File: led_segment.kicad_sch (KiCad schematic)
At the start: 8 parts, among them Q7 BC857

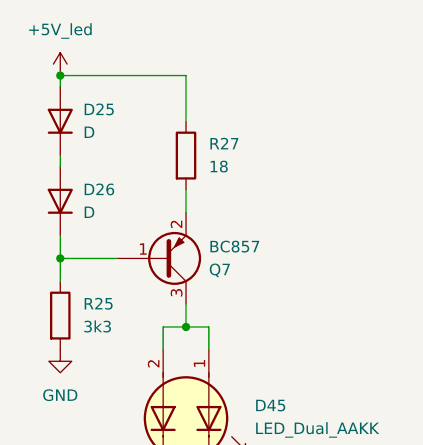
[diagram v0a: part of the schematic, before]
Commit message: current source diodes specified
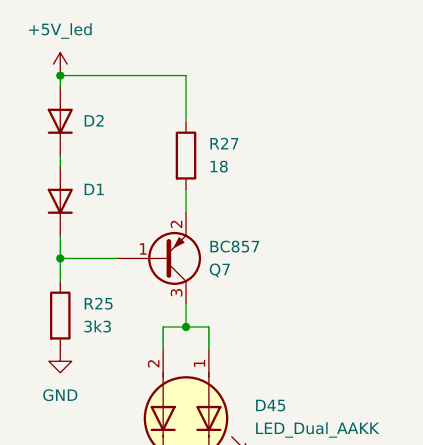
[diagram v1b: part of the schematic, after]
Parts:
- removed D25, D26: D, Diode_SMD:D_0603_1608Metric, symbol Device:D
- added D1, D2: 1N4148, Diode_THT:D_DO-35_SOD27_P7.62mm_Horizontal, symbol Diode:1N4148
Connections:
- net +5V_led: now also D2.2 (A)
- net at Q7.1 (B), R25.1: now also D1.1 (K)
- new net: D1.2 (A), D2.1 (K)

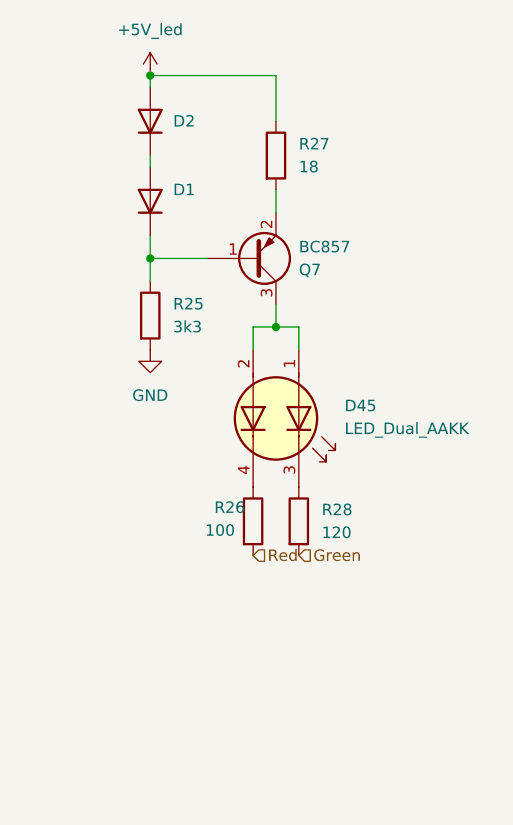
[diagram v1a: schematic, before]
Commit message: Schematic sites change
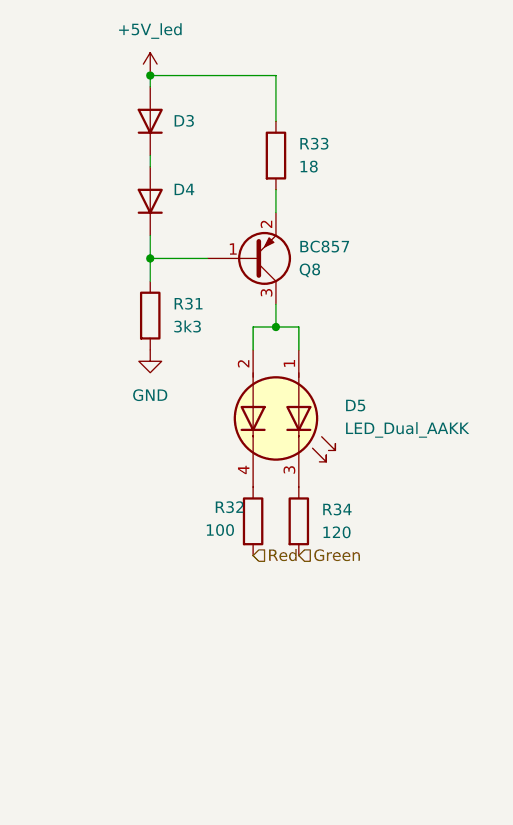
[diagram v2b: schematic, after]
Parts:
- D3: renamed from D2; footprint Diode_THT:D_DO-35_SOD27_P7.62mm_Horizontal -> Diode_SMD:D_SOD-123
- D4: renamed from D1; footprint Diode_THT:D_DO-35_SOD27_P7.62mm_Horizontal -> Diode_SMD:D_SOD-123
- renumbered D45 to D5, Q7 to Q8, R25 to R31, R26 to R32, R27 to R33, R28 to R34

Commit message: mos leds drivers
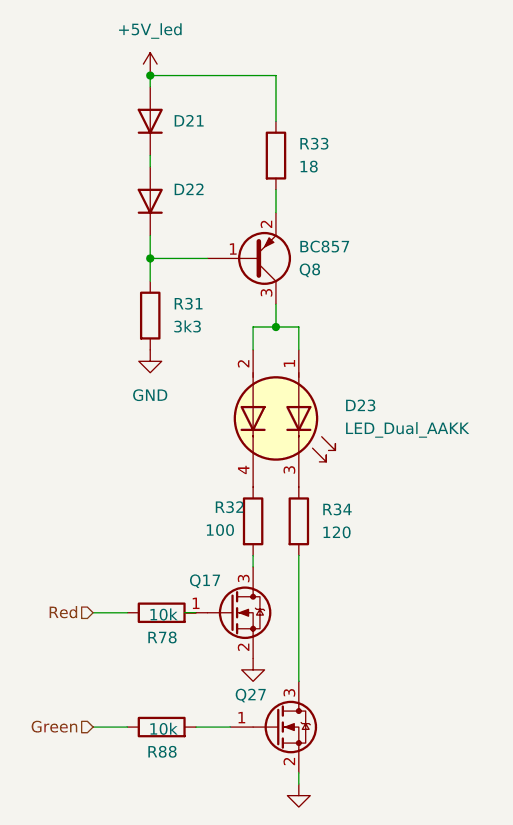
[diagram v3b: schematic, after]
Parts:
- added Q17, Q27: 2N7002H, Package_TO_SOT_SMD:SOT-23, symbol Transistor_FET:2N7002H
- added R78, R88: 10k, Resistor_SMD:R_0603_1608Metric, symbol Device:R
- renumbered D3 to D21, D4 to D22, D5 to D23
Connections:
- net GND: now also Q17.2 (S), Q27.2 (S)
- net Green: now also R88.1; no longer R34.2
- net Red: now also R78.1; no longer R32.2
- new net: Q17.1 (G), R78.2
- new net: Q17.3 (D), R32.2
- new net: Q27.1 (G), R88.2
- new net: Q27.3 (D), R34.2

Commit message: New current source and external mosfet keys for leds
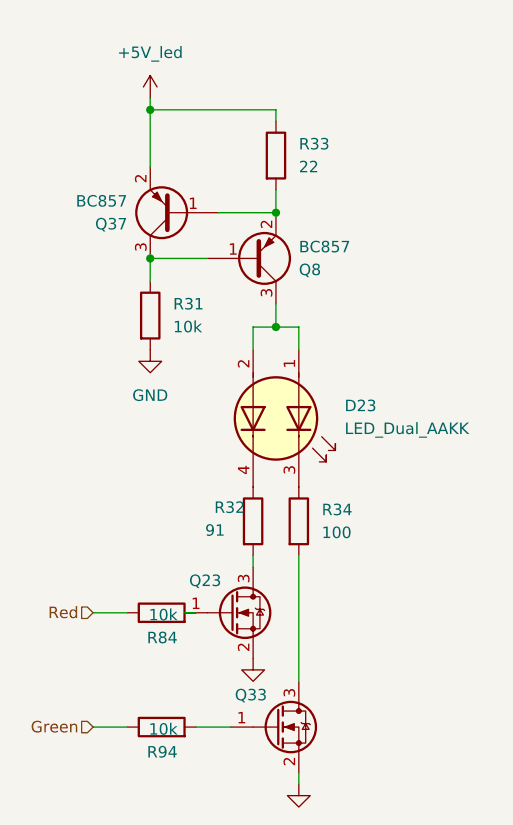
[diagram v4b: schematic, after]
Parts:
- removed D21, D22: 1N4148, Diode_SMD:D_SOD-123, symbol Diode:1N4148
- added Q37: BC857, Package_TO_SOT_SMD:SOT-23, symbol Transistor_BJT:BC857
- R31: value 3k3 -> 10k
- R32: value 100 -> 91
- R33: value 18 -> 22
- R34: value 120 -> 100
- renumbered Q17 to Q23, Q27 to Q33, R78 to R84, R88 to R94
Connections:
- net +5V_led: now also Q37.2 (E)
- net at Q8.1 (B), R31.1: now also Q37.3 (C)
- net at Q8.2 (E), R33.2: now also Q37.1 (B)

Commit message: Nets rules
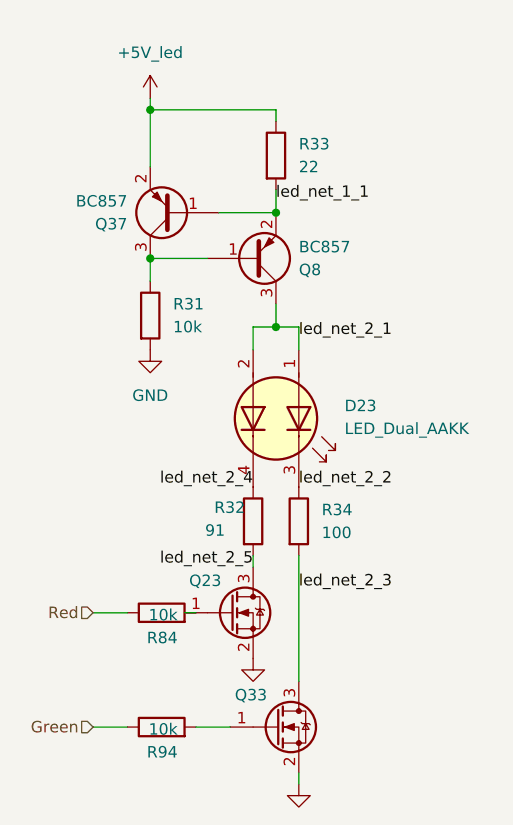
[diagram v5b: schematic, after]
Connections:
- net led_net_2_5: now reaches Q23.3 (D), R32.2
- net led_net_1_1: now reaches Q37.1 (B), Q8.2 (E), R33.2
- net led_net_2_1: now reaches D23.1 (A1), D23.2 (A2), Q8.3 (C)
- net led_net_2_2: now reaches D23.3 (K1), R34.1
- net led_net_2_4: now reaches D23.4 (K2), R32.1
- net led_net_2_3: now reaches Q33.3 (D), R34.2
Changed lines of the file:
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@@
+		)
+	)
+	(label "led_net_2_5"
+		(at 113.03 95.25 180)
+		(fields_autoplaced yes)
+		(effects
+			(font
+				(size 1.27 1.27)
+			)
+			(justify right bottom)
+		)
+	)
+	(label "led_net_2_3"
+		(at 118.11 97.79 0)
+		(fields_autoplaced yes)
+		(effects
+			(font
+				(size 1.27 1.27)
+			)
+			(justify left bottom)
+		)
+	)
+	(label "led_net_2_2"
+		(at 118.11 86.36 0)
+		(fields_autoplaced yes)
+		(effects
+			(font
+				(size 1.27 1.27)
+			)
+			(justify left bottom)
+		)
+	)
+	(label "led_net_2_4"
+		(at 113.03 86.36 180)
+		(fields_autoplaced yes)
+		(effects
+			(font
+				(size 1.27 1.27)
+			)
+			(justify right bottom)
+		)
+	)
+	(label "led_net_1_1"
+		(at 115.57 54.61 0)
+		(fields_autoplaced yes)
+		(effects
+			(font
+				(size 1.27 1.27)
+			)
+			(justify left bottom)
+		)
+	)
+	(label "led_net_2_1"
+		(at 118.11 69.85 0)
+		(fields_autoplaced yes)
+		(effects
+			(font
+				(size 1.27 1.27)
+			)
+			(justify left bottom)
 		)
 	)

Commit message: Shifting registers
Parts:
- removed Q23, Q33: 2N7002H, Package_TO_SOT_SMD:SOT-23, symbol Transistor_FET:2N7002H
- removed R84, R94: 10k, Resistor_SMD:R_0603_1608Metric, symbol Device:R
- renumbered D23 to D3, Q37 to Q2, Q8 to Q4, R32 to R10, R33 to R11, R34 to R12, R31 to R7
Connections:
- net led_net_2_3 is gone; now on net Green: R12.2
- net led_net_2_5 is gone; now on net Red: R10.2

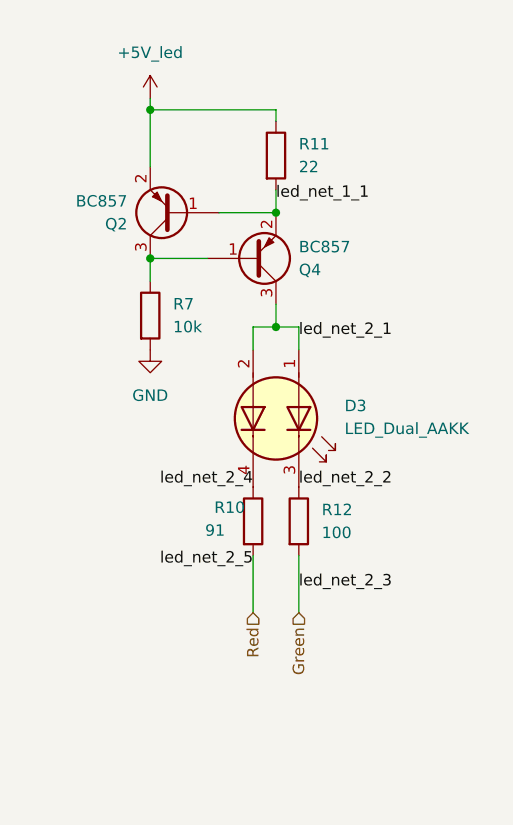
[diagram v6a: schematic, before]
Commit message: Step_down 5v
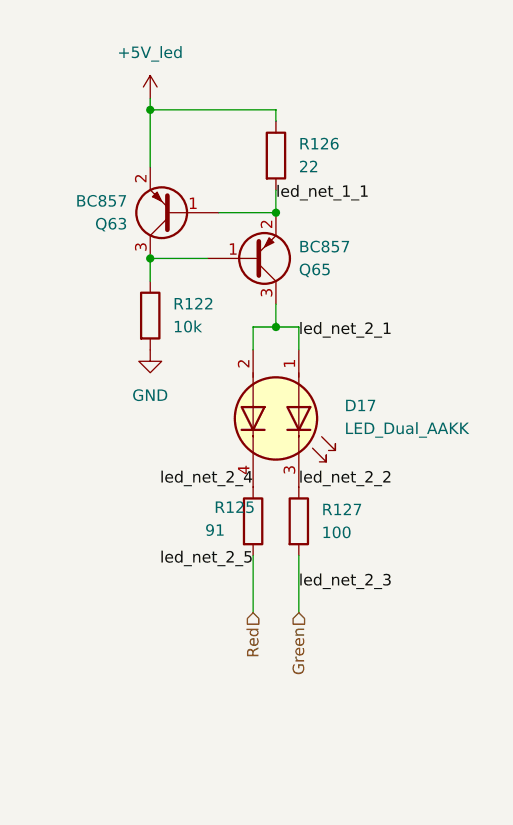
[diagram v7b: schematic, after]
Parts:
- renumbered D3 to D17, Q2 to Q63, Q4 to Q65, R7 to R122, R10 to R125, R11 to R126, R12 to R127
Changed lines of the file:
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@@
 		(dnp no)
 		(fields_autoplaced yes)
-		(property "Reference" "#PWR09"
+		(property "Reference" "#PWR0106"
 			(at 101.6 77.47 0)
 			(effects
@@
 		(on_board yes)
 		(dnp no)
-		(property "Reference" "Q4"
+		(property "Reference" "Q65"
 			(at 118.11 62.2301 0)
 			(effects
@@
 		(on_board yes)
 		(dnp no)
-		(property "Reference" "Q2"
+		(property "Reference" "Q63"
 			(at 99.06 57.1501 0)
 			(effects
@@
 		(dnp no)
 		(fields_autoplaced yes)
-		(property "Reference" "D3"
+		(property "Reference" "D17"
 			(at 123.19 77.3429 90)
 			(effects
@@
 		(on_board yes)
 		(dnp no)
-		(property "Reference" "R10"
+		(property "Reference" "R125"
 			(at 108.712 88.646 0)
 			(effects
@@
 		(dnp no)
 		(fields_autoplaced yes)
-		(property "Reference" "R12"
+		(property "Reference" "R127"
 			(at 120.65 88.8999 0)
 			(effects
@@
 		(dnp no)
 		(fields_autoplaced yes)
-		(property "Reference" "R11"
+		(property "Reference" "R126"
 			(at 118.11 48.2599 0)
 			(effects
@@
 		(dnp no)
 		(fields_autoplaced yes)
-		(property "Reference" "R7"
+		(property "Reference" "R122"
 			(at 104.14 66.0399 0)
 			(effects
@@
 		(dnp no)
 		(fields_autoplaced yes)
-		(property "Reference" "#PWR08"
+		(property "Reference" "#PWR0105"
 			(at 101.6 46.99 0)
 			(effects

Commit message: New template
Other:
- company: (none) -> STAPsystem
- title: (none) -> RPM meter LED
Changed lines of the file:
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@@
 	(generator_version "8.0")
 	(paper "A4")
+	(title_block
+		(title "RPM meter LED")
+		(date "2024-11-26")
+		(rev "v1.0")
+		(company "STAPsystem")
+	)
 	(junction
 		(at 115.57 55.88)
